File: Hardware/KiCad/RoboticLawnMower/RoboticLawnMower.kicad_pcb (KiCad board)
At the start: 2 copper layers, 100.1 x 100 mm, 143 parts, among them J1 Conn_01x08, J10 Conn_01x02, J11 Conn_01x02, J12 Conn_02x05_Row_Letter_Last, J13 Conn_01x04, J14 Conn_01x06, J15 Conn_01x06, J16 Conn_01x06, J18 Conn_02x05_Row_Letter_Last, J2 Conn_01x08, J3 Conn_01x08, J4 Conn_01x08, J5 Conn_01x08, J6 Conn_01x04, J7 Conn_01x04, J8 Conn_01x04, J9 Conn_01x04, Q1 BSS123, Q2 BSS123, Q3 Si7141DP, Q4 Si7141DP, U1 INA233, U10 INA233, U11 INA233, U12 INA233, U13 INA233, U14 PCA9547BS, U2 AVR128DB48x-xPT, U4 PCA9685PW, U5 AVR128DB48x-xPT, U6 LT1129-3.3_SOT223, U7 TSR_1-2450, U8 ADS1115IDGS, U9 ADS1115IDGS, Y1 32.768kHz, Y2 32.768kHz

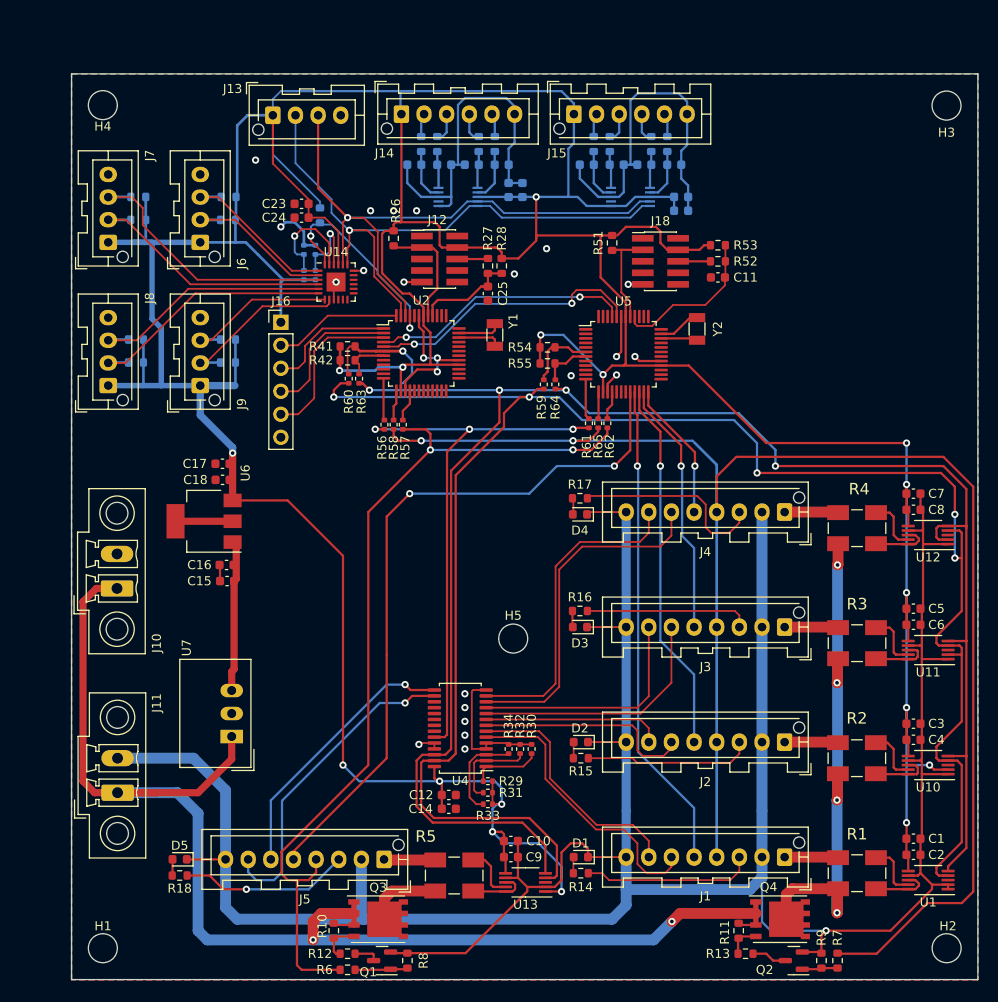
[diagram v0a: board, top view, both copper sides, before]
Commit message: Schaltplan und Layout änderung
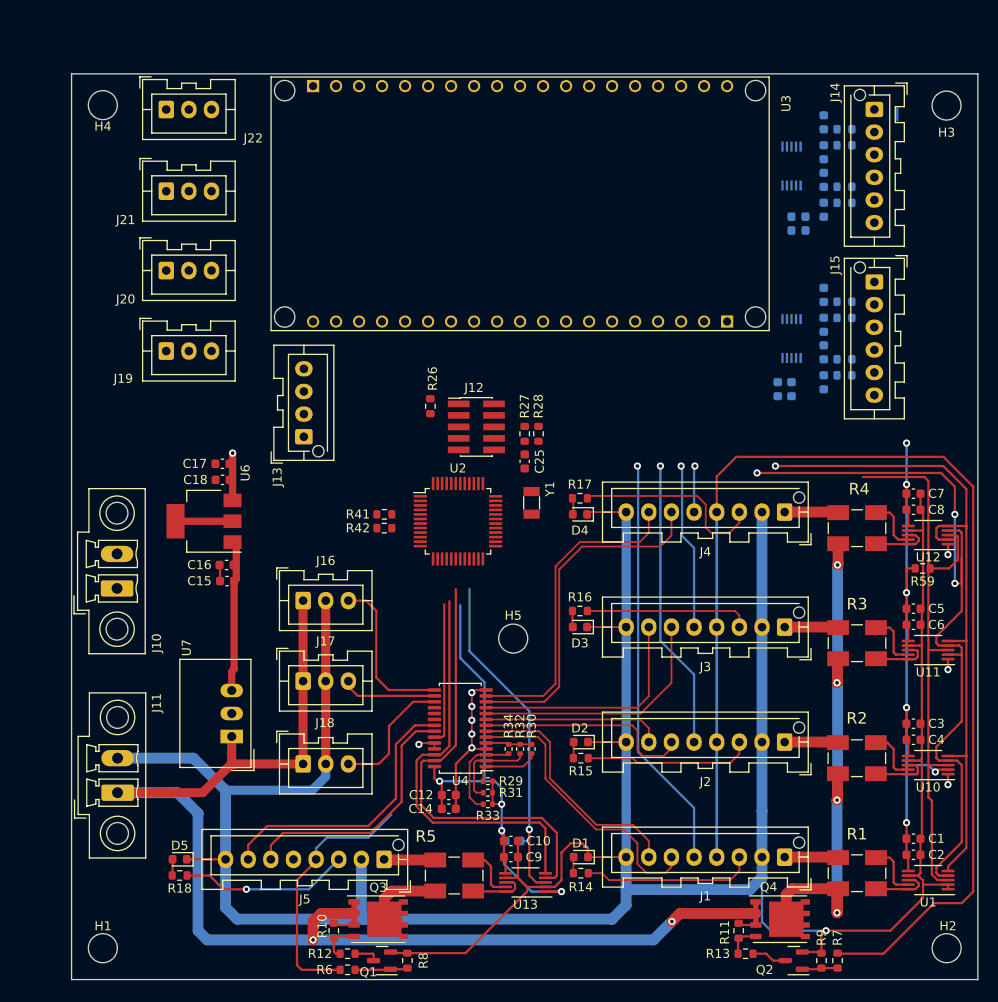
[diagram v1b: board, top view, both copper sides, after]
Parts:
- removed C11: 5p6, Capacitor_SMD:C_0603_1608Metric
- removed C23: 100n, Capacitor_SMD:C_0603_1608Metric
- removed C24: 1u, Capacitor_SMD:C_0603_1608Metric
- removed J6, J7, J8, J9: Conn_01x04, Connector_JST:JST_XA_B04B-XASK-1-A_1x04_P2.50mm_Vertical
- removed R19: 10K, Resistor_SMD:R_0603_1608Metric
- removed R20, R21, R22, R23, R24, R25, R35, R36, R54, R55: 4k7, Resistor_SMD:R_0603_1608Metric
- removed R37, R39: 10K, Resistor_SMD:R_0402_1005Metric
- removed R38, R40, R56, R57, R58, R60, R63: N.P., Resistor_SMD:R_0402_1005Metric
- removed R51, R53: 47K, Resistor_SMD:R_0603_1608Metric
- removed R52: 33R, Resistor_SMD:R_0603_1608Metric
- removed R62, R64, R65: 10R, Resistor_SMD:R_0402_1005Metric
- removed U14: PCA9547BS, Package_DFN_QFN:HVQFN-24-1EP_4x4mm_P0.5mm_EP2.1x2.1mm
- removed U5: AVR128DB48x-xPT, Package_QFP:TQFP-48_7x7mm_P0.5mm
- removed Y2: 32.768kHz, Crystal:Crystal_SMD_3215-2Pin_3.2x1.5mm
- added J17: Conn_01x03, Connector_JST:JST_XA_B03B-XASK-1_1x03_P2.50mm_Vertical, F.Cu at (114.5, 110.1)
- added J19: Conn_01x03, Connector_JST:JST_XA_B03B-XASK-1_1x03_P2.50mm_Vertical, F.Cu at (99.4, 73.7)
- added J20: Conn_01x03, Connector_JST:JST_XA_B03B-XASK-1_1x03_P2.50mm_Vertical, F.Cu at (99.4, 64.8)
- added J21: Conn_01x03, Connector_JST:JST_XA_B03B-XASK-1_1x03_P2.50mm_Vertical, F.Cu at (99.4, 56.0)
- added J22: Conn_01x03, Connector_JST:JST_XA_B03B-XASK-1_1x03_P2.50mm_Vertical, F.Cu at (99.4, 47.0)
- added U3: ESP32_NODEMCU, ESP32_NODEMCU:MODULE_ESP32_NODEMCU, F.Cu at (138.4, 57.4)
- J16: value Conn_01x06 -> Conn_01x03; footprint Connector_PinHeader_2.54mm:PinHeader_1x06_P2.54mm_Vertical -> Connector_JST:JST_XA_B03B-XASK-1_1x03_P2.50mm_Vertical
- J18: value Conn_02x05_Row_Letter_Last -> Conn_01x03; footprint Connector_PinHeader_1.27mm:PinHeader_2x05_P1.27mm_Vertical_SMD -> Connector_JST:JST_XA_B03B-XASK-1_1x03_P2.50mm_Vertical
- R59: value 10R -> 4k7; footprint Resistor_SMD:R_0402_1005Metric -> Resistor_SMD:R_0603_1608Metric
- R61: value 10R -> 4k7; footprint Resistor_SMD:R_0402_1005Metric -> Resistor_SMD:R_0603_1608Metric; moved to B.Cu
- moved J18 68.1 mm to (114.5, 119.3)
- moved J14 52.2 mm to (177.5, 47.0), turned to -90 degrees
- moved R61 46.9 mm to (137.7, 127.8), turned to 180 degrees
- moved R43 46.8 mm to (174.2, 49.2), turned to 0 degrees
- moved R59 46.5 mm to (182.9, 97.7), turned to 180 degrees
- moved C32 45.5 mm to (172.0, 48.4), turned to 90 degrees
- moved R44 45.0 mm to (174.2, 50.9), turned to 0 degrees
- moved C30 41.9 mm to (172.0, 51.7), turned to -90 degrees
- moved R45 40.7 mm to (174.2, 55.5), turned to 0 degrees
- moved R46 39.2 mm to (174.2, 57.3), turned to 0 degrees
- moved C28 38.9 mm to (172.0, 54.8), turned to 90 degrees
- moved J15 38.0 mm to (177.5, 66.0), turned to -90 degrees
- moved U8 37.0 mm to (168.4, 53.2), turned to -90 degrees
- moved C26 35.9 mm to (172.0, 58.1), turned to -90 degrees
- moved J13 35.7 mm to (114.6, 83.1), turned to 90 degrees
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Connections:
- J10 pad 1: +BATT -> /charge/POWER_IN
- J16 pad 1: +3.3V -> +BATT
- J16 pad 2: /uC/UART_0_TXD -> GND
- J16 pad 3: /uC/UART_0_RXD -> /PWM_CH_8
- J18 pad 1: unconnected-(J18-Pad1) -> +BATT
- J18 pad 3: /uC/AVR_UPDI_1 -> /PWM_CH_10
- J5 pad 6: /PWM_CH_8 -> /PWM_CH_15
- J5 pad 7: /PWM_CH_9 -> /PWM_CH_14
- R41 pad 1: Net-(R41-Pad1) -> /Motor_M1/SDA
- R42 pad 1: Net-(R42-Pad1) -> /Motor_M1/SCL
- R59 pad 1: Net-(R54-Pad1) -> /Motor_M1/~{Alert}
- R59 pad 2: /Motor_M1/SDA -> +3.3V
- R61 pad 1: Net-(R61-Pad1) -> /Motor_M5/~{Alert}
- R61 pad 2: /i2c_io_pwm/~{PCA_9685_OE} -> +3.3V
- U10 pad 3: /Motor_M2/~{Alert} -> /Motor_M1/~{Alert}
- U11 pad 3: /Motor_M3/~{Alert} -> /Motor_M1/~{Alert}
- U12 pad 3: /Motor_M4/~{Alert} -> /Motor_M1/~{Alert}
- U2 pad 1: /uC/UART_0_RXD -> /WLAN/WLAN_TxD
- U2 pad 12: Net-(R56-Pad1) -> /i2c_io_pwm/~{PCA_9685_OE}
- U2 pad 13: Net-(R58-Pad1) -> /Motor_M1..4_EN
- U2 pad 16: Net-(R57-Pad1) -> /Motor_M5_EN
- U2 pad 17: unconnected-(U2-Pad17) -> /Motor_M1/~{Alert}
- U2 pad 18: unconnected-(U2-Pad18) -> /Motor_M5/~{Alert}
- U2 pad 2: /uC/UART_0_XCK -> /WLAN/UART_0_XCK
- U2 pad 3: /uC/UART_0_XDIR -> /WLAN/UART_0_XDIR
- U2 pad 30: unconnected-(U2-Pad30) -> /Sensor/RainSensor
- U2 pad 31: unconnected-(U2-Pad31) -> /Sensor/DistanceSensor_00
- U2 pad 32: unconnected-(U2-Pad32) -> /Sensor/DistanceSensor_01
- U2 pad 33: unconnected-(U2-Pad33) -> /Sensor/DistanceSensor_02
- U2 pad 4: Net-(U2-Pad4) -> unconnected-(U2-Pad4)
- U2 pad 45: /i2c_smb_mux/~{RESET} -> unconnected-(U2-Pad45)
- U2 pad 48: /uC/UART_0_TXD -> /WLAN/WLAN_RxD
- U2 pad 5: Net-(U2-Pad5) -> unconnected-(U2-Pad5)
- U2 pad 6: Net-(R41-Pad1) -> /Motor_M1/SDA
- U2 pad 7: Net-(R42-Pad1) -> /Motor_M1/SCL
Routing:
- net +3.3V: track 543.3 -> 137.2 mm, vias 17 -> 11
- net GND: track 471.5 -> 389.9 mm, vias 25 -> 10
- net /Motor_M5/MOT_SIGNAL: track 78.5 -> 0.88 mm, vias 2 -> 0
- net /Motor_M1/SCL: track 197.4 -> 120.5 mm, vias 4 -> 1
- net /Motor_M1/SDA: track 211.5 -> 135.8 mm, vias 5 -> 3
- net /Motor_M5_EN: track 100.5 -> 28.7 mm, vias 2 -> 0
- net /i2c_analog/SDA: track 67.7 -> 0.00 mm, vias 1 -> 0
- net /i2c_analog/SCL: track 67.4 -> 0.00 mm, vias 1 -> 0
- net /Motor_M1/~{Alert}: track 0.00 -> 64.7 mm
- net /Motor_M1..4_EN: track 181.8 -> 135.2 mm, vias 2 -> 0
- net /i2c_io_pwm/~{PCA_9685_OE}: track 60.9 -> 15.7 mm, vias 3 -> 0
- net /Motor_M5/~{Alert}: track 0.00 -> 38.8 mm, vias 0 -> 1
- net /PWM_CH_14: track 0.00 -> 31.1 mm
- net Net-(U2-Pad5): track 30.8 -> 0.00 mm, vias 2 -> 0
- net Net-(J7-Pad3): track 30.6 -> 0.00 mm
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- removed copper zone on B.Cu, net GND
- removed copper zone on F.Cu, net GND

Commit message: Layout
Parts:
- J1, J2, J3, J4, J5: footprint Connector_JST:JST_XA_B08B-XASK-1-A_1x08_P2.50mm_Vertical -> Connector_JST:JST_XA_B08B-XASK-1_1x08_P2.50mm_Vertical
- J13: footprint Connector_JST:JST_XA_B04B-XASK-1-A_1x04_P2.50mm_Vertical -> Connector_JST:JST_XA_B04B-XASK-1_1x04_P2.50mm_Vertical
- J14, J15: footprint Connector_JST:JST_XA_B06B-XASK-1-A_1x06_P2.50mm_Vertical -> Connector_JST:JST_XA_B06B-XASK-1_1x06_P2.50mm_Vertical
- U3: value ESP32_NODEMCU -> mini_esp32; footprint ESP32_NODEMCU:MODULE_ESP32_NODEMCU -> ESP32_mini:ESP32_mini
- moved J14 63.4 mm to (114.1, 47.1), turned to 0 degrees
- moved R43 57.9 mm to (116.3, 50.4), turned to 90 degrees
- moved C32 56.6 mm to (115.6, 52.7), turned to 180 degrees
- moved R44 56.1 mm to (118.1, 50.4), turned to 90 degrees
- moved C30 53.1 mm to (118.9, 52.7), turned to 0 degrees
- moved R45 51.8 mm to (122.7, 50.4), turned to 90 degrees
- moved R46 50.3 mm to (124.5, 50.4), turned to 90 degrees
- moved C28 50.1 mm to (121.9, 52.7), turned to 180 degrees
- moved J15 48.2 mm to (133.2, 47.1), turned to 0 degrees
- moved U8 48.1 mm to (120.4, 56.3), turned to 0 degrees
- moved C26 47.0 mm to (125.2, 52.7), turned to 0 degrees
- moved C19 43.3 mm to (126.0, 55.5), turned to 90 degrees
- moved R47 42.7 mm to (135.4, 50.4), turned to 90 degrees
- moved C21 41.9 mm to (127.5, 55.5), turned to 90 degrees
- moved R48 41.9 mm to (137.2, 50.4), turned to 90 degrees
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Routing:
- net +3.3V: track 137.2 -> 210.1 mm, vias 11 -> 12
- net /Motor_M1/SDA: track 135.8 -> 205.9 mm, vias 3 -> 5
- net /Sensor/DistanceSensor_02: track 0.00 -> 69.4 mm, vias 0 -> 1
- net /Motor_M1/SCL: track 120.5 -> 186.7 mm, vias 1 -> 3
- net /Sensor/DistanceSensor_01: track 0.00 -> 60.7 mm, vias 0 -> 1
- net /Motor_M1/~{Alert}: track 64.7 -> 124.5 mm, vias 0 -> 2
- net /WLAN/UART_0_XDIR: track 0.00 -> 57.6 mm
- net /Sensor/DistanceSensor_00: track 0.00 -> 51.5 mm, vias 0 -> 1
- net /WLAN/WLAN_RxD: track 0.00 -> 50.1 mm
- net /WLAN/UART_0_XCK: track 0.00 -> 48.2 mm
- net /WLAN/WLAN_TxD: track 0.00 -> 46.2 mm
- net /Sensor/RainSensor: track 0.00 -> 43.2 mm, vias 0 -> 1
- net /Motor_M1..4_EN: track 135.2 -> 169.4 mm, vias 0 -> 3
- net /Motor_M5_EN: track 28.7 -> 59.4 mm, vias 0 -> 1
- net GND: track 389.9 -> 420.5 mm
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
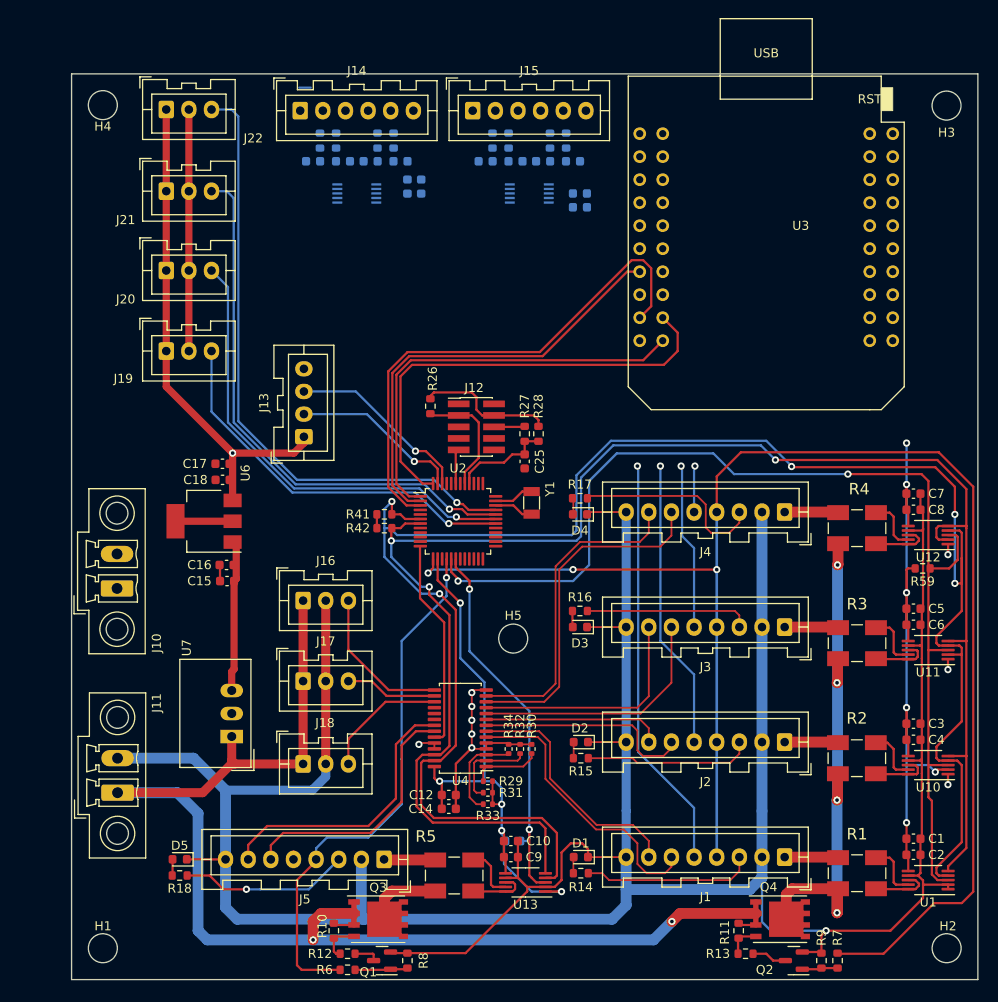
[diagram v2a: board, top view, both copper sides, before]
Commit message: Schaltplan & Layout Änderung
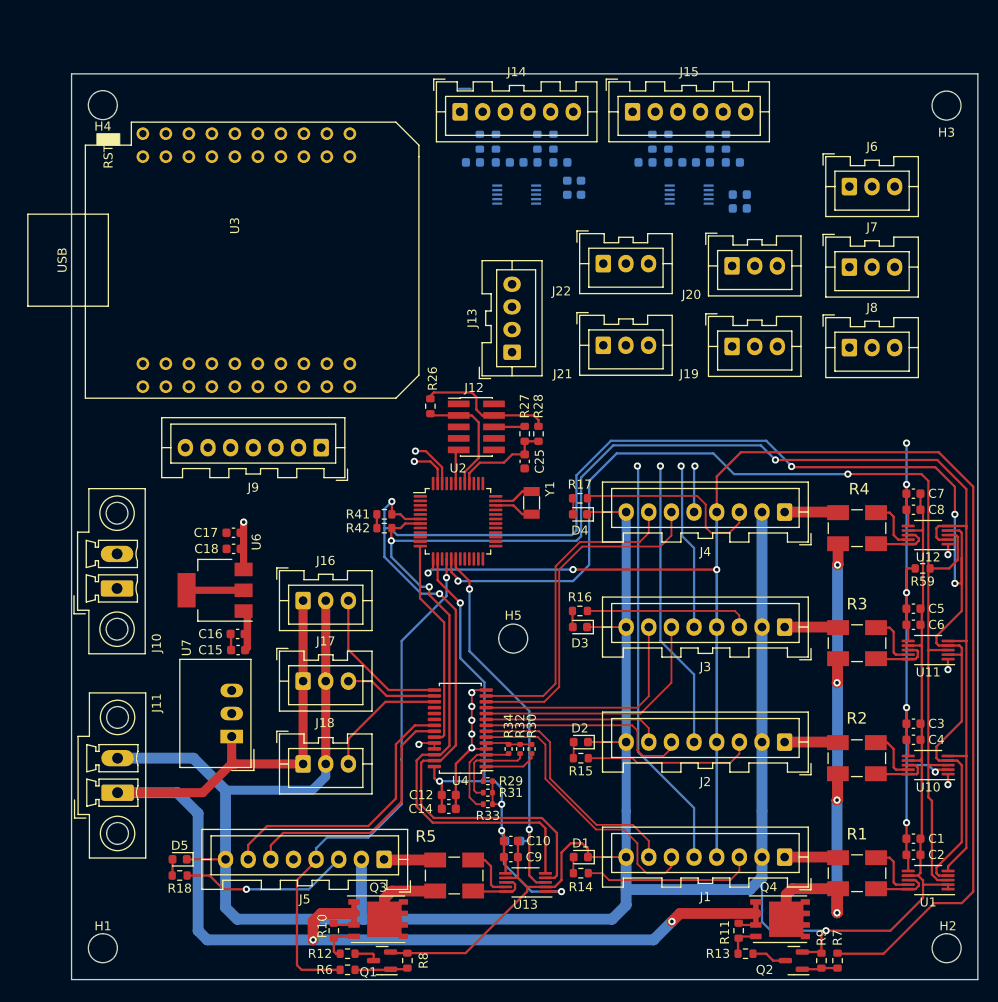
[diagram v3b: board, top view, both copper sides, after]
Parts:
- added J6: Coll 00, Connector_JST:JST_XA_B03B-XASK-1_1x03_P2.50mm_Vertical, F.Cu at (174.8, 55.5)
- added J7: Coll 01, Connector_JST:JST_XA_B03B-XASK-1_1x03_P2.50mm_Vertical, F.Cu at (174.8, 64.4)
- added J8: Coll 02, Connector_JST:JST_XA_B03B-XASK-1_1x03_P2.50mm_Vertical, F.Cu at (174.8, 73.3)
- added J9: GPS, Connector_JST:JST_XA_B07B-XASK-1_1x07_P2.50mm_Vertical, F.Cu at (116.5, 84.3)
- J1, J2, J3, J4, J5: value Conn_01x08 -> MOTOR
- J13: value Conn_01x04 -> I2C 0
- J14: value Conn_01x06 -> ADC 1
- J15: value Conn_01x06 -> ADC 2
- J19: value Conn_01x03 -> RAIN
- J20: value Conn_01x03 -> Dist 00
- J21: value Conn_01x03 -> Dist 01
- J22: value Conn_01x03 -> Dist 02
- moved J19 62.5 mm to (161.8, 73.2)
- moved J20 62.5 mm to (161.8, 64.3)
- moved U3 57.5 mm to (108.2, 63.6), turned to -90 degrees
- moved J21 51.2 mm to (147.6, 73.0)
- moved J22 51.2 mm to (147.6, 64.0)
- moved J13 24.8 mm to (137.5, 73.8)
- moved C20 17.7 mm to (162.7, 57.9)
- moved C22 17.7 mm to (162.7, 56.4)
- moved C27 17.7 mm to (161.9, 52.8)
- moved C32 17.7 mm to (133.2, 52.8)
- moved R43 17.7 mm to (134.0, 50.5)
- moved R50 17.7 mm to (161.2, 50.5)
- moved C19 17.7 mm to (143.6, 55.6)
- moved C21 17.7 mm to (145.2, 55.6)
- moved C26 17.7 mm to (142.9, 52.8)
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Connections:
- U2 pad 10: unconnected-(U2-Pad10) -> /GPS/GPS_RESET_EN
- U2 pad 11: unconnected-(U2-Pad11) -> /GPS/GPS_PPS
- U2 pad 24: unconnected-(U2-Pad24) -> /Sensor/Collision_Sensor_02
- U2 pad 25: unconnected-(U2-Pad25) -> /Sensor/Collision_Sensor_01
- U2 pad 26: unconnected-(U2-Pad26) -> /Sensor/Collision_Sensor_00
- U2 pad 30: /Sensor/RainSensor -> /uC/SPI_0_MOSI
- U2 pad 31: /Sensor/DistanceSensor_00 -> /uC/SPI_0_MISO
- U2 pad 32: /Sensor/DistanceSensor_01 -> /uC/SPI_0_SCLK
- U2 pad 33: /Sensor/DistanceSensor_02 -> /uC/SPI_0_CS
- U2 pad 36: unconnected-(U2-Pad36) -> /Sensor/RainSensor
- U2 pad 37: unconnected-(U2-Pad37) -> /Sensor/DistanceSensor_00
- U2 pad 38: unconnected-(U2-Pad38) -> /Sensor/DistanceSensor_01
- U2 pad 39: unconnected-(U2-Pad39) -> /Sensor/DistanceSensor_02
- U2 pad 8: unconnected-(U2-Pad8) -> /GPS/GPS_UART_3_TXD
- U2 pad 9: unconnected-(U2-Pad9) -> /GPS/GPS_UART_3_RXD
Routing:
- net /Sensor/DistanceSensor_02: track 69.4 -> 0.00 mm, vias 1 -> 0
- net /Sensor/DistanceSensor_01: track 60.7 -> 0.00 mm, vias 1 -> 0
- net /WLAN/UART_0_XDIR: track 57.6 -> 0.00 mm
- net /Sensor/DistanceSensor_00: track 51.5 -> 0.00 mm, vias 1 -> 0
- net /WLAN/WLAN_RxD: track 50.1 -> 0.00 mm
- net +3.3V: track 210.1 -> 160.1 mm
- net /WLAN/UART_0_XCK: track 48.2 -> 0.00 mm
- net /WLAN/WLAN_TxD: track 46.2 -> 0.00 mm
- net /Sensor/RainSensor: track 43.2 -> 0.00 mm, vias 1 -> 0
- net GND: track 420.5 -> 393.8 mm
- net /i2c_analog/SDA: track 20.5 -> 5.48 mm
- net /i2c_analog/SCL: track 18.9 -> 4.55 mm
- net +5V: track 16.9 -> 4.70 mm
